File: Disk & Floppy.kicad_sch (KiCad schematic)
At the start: 13 parts, among them J7 Internal FDD, U18 74LS74, U19 74LS244, U20 74LS245, U21 74LS74, U22 74LS06, X1 8.010613MHz

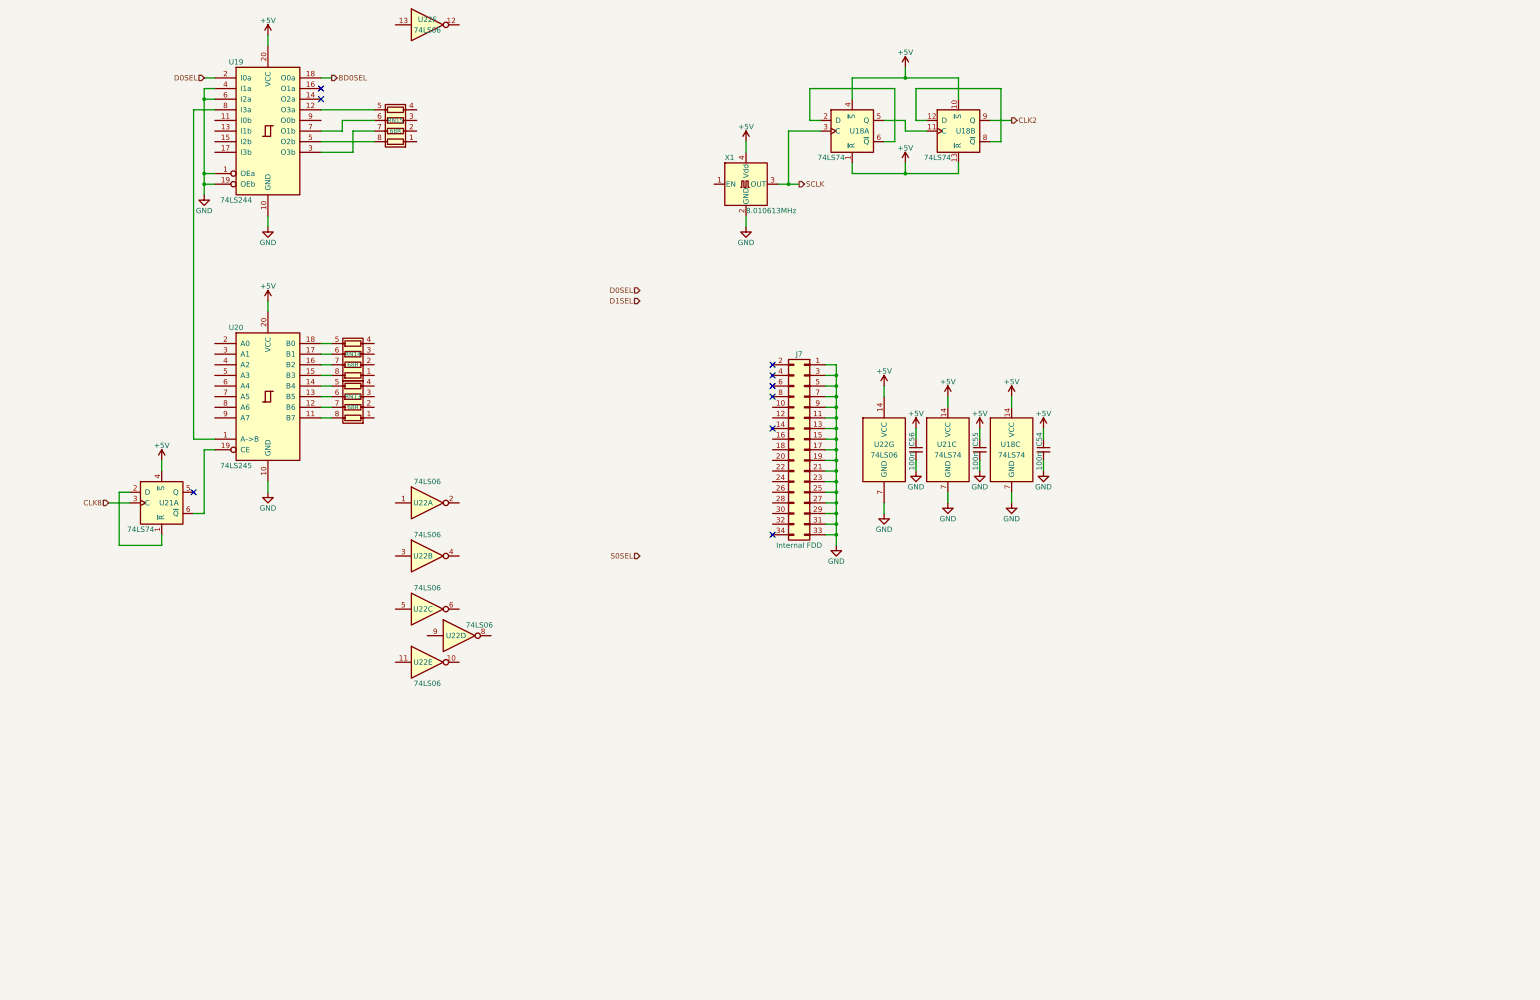
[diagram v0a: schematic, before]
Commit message: motherboard: Added the HDD and FDD controller logic to the schematic
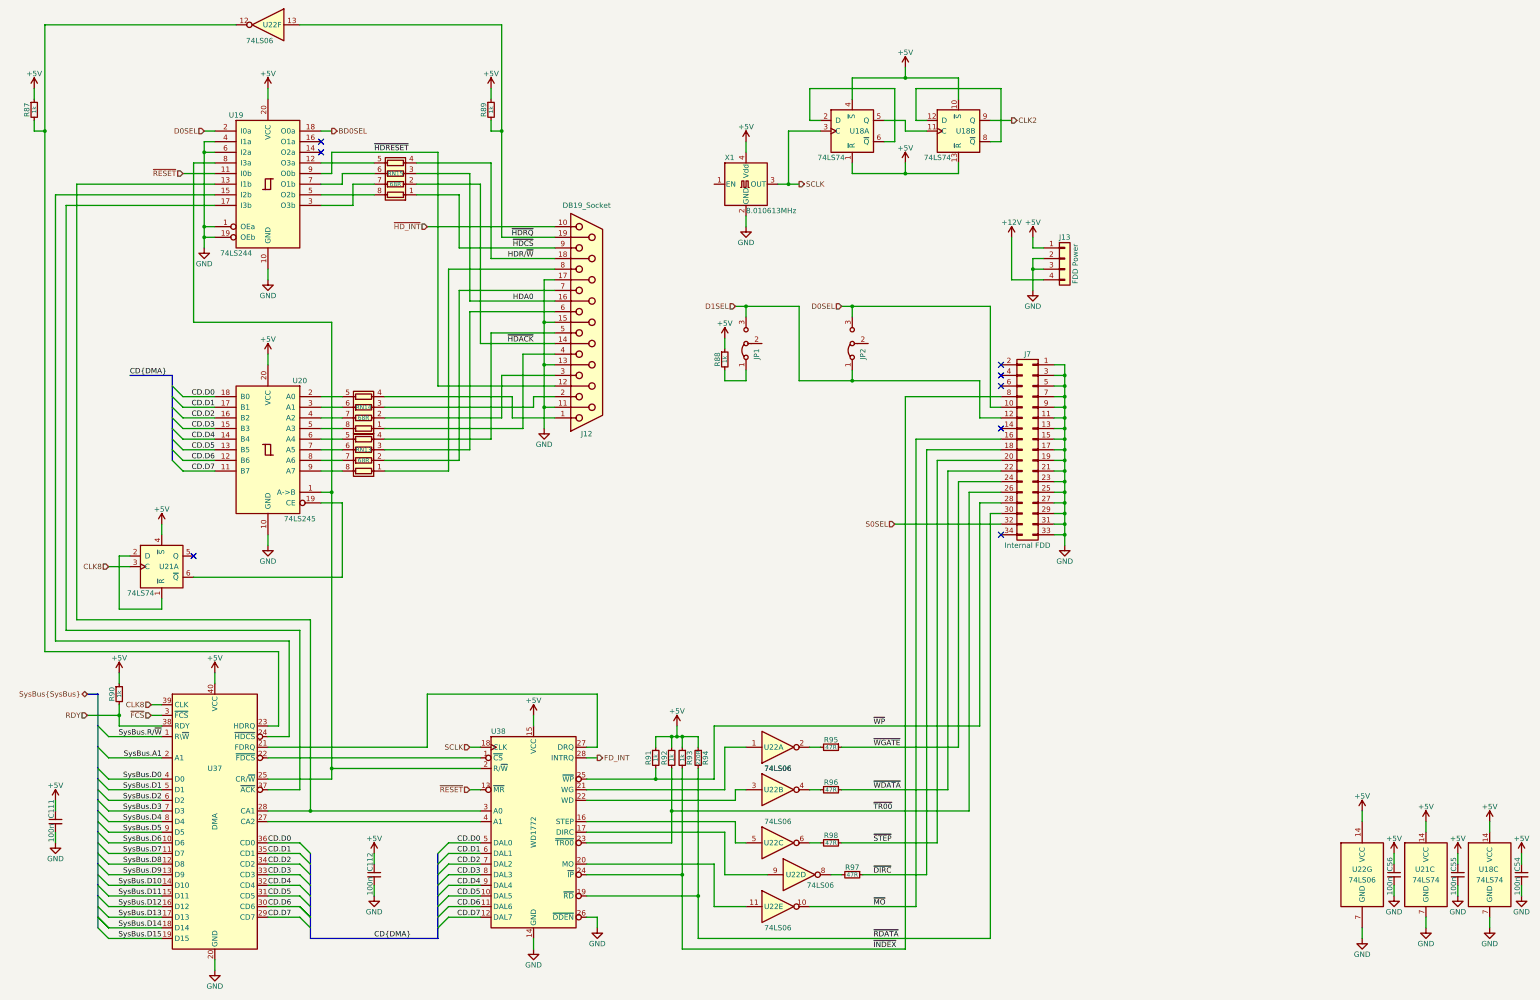
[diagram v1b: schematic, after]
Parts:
- added C111, C112: 100n, rhais_rcl:C0603, symbol Device:C_Small
- added J12: DB19_Socket, symbol dragonSTe:DB19_Socket
- added J13: FDD Power, symbol Connector_Generic:Conn_01x04
- added JP1, JP2: Jumper_3_Bridged12, symbol Jumper:Jumper_3_Bridged12
- added R87, R88, R89, R90, R91, R92, R93: 1k, rhais_rcl:R0603, symbol Device:R_Small
- added R94: 220R, rhais_rcl:R0603, symbol Device:R_Small
- added R95, R96, R97, R98: 47R, rhais_rcl:R0603, symbol Device:R_Small
- added U37: DMA, Package_DIP:DIP-40_W15.24mm_Socket, symbol dragonSTe:DMA
- added U38: WD1772, Package_DIP:DIP-28_W15.24mm_Socket, symbol dragonSTe:WD1772
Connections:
- net +5V: now also C111.1, C112.1, J13.1 (Pin_1), R87.1, R88.1, R89.1, R90.1, R91.1, R92.1, R93.1, R94.1, U37.40 (VCC), U38.15 (VCC)
- net CLK8: now also U37.39 (CLK)
- net D0SEL: now also J7.10 (Pin_10), JP2.3 (B)
- net D1SEL: now also J7.12 (Pin_12), JP1.3 (B), JP2.1 (A)
- net GND: now also C111.2, C112.2, J12.11, J12.13, J12.15 (P15), J12.17 (P17), J13.2 (Pin_2), J13.3 (Pin_3), U37.20 (GND), U37.28 (CA1), U38.14 (GND), U38.26 (~{DDEN})
- net S0SEL: now also J7.32 (Pin_32)
- net SCLK: now also U38.18 (CLK)
- net at U22.3: now also U38.22 (WD)
- net at U22.4: now also R96.2
- net ~{RESET}: now reaches U19.11 (I0b)
- net ~{RESET}: now also U38.13 (~{MR})
- net at U19.13 (I1b): now also U37.28 (CA1), U38.3 (A0)
- net at U19.15 (I2b): now also U37.24 (~{HDCS})
- net at U19.17 (I3b): now also U37.37 (~{ACK})
- net at U19.8 (I3a), U20.1 (A->B): now also U37.25 (CR/~{W}), U38.2 (R/~{W})
- net ~{HDRESET}: now reaches U19.9 (O0b)
- net ~{HDRESET}: now also J12.12
- net at RN13.8 (R1.2): now also U20.9 (A7); no longer U20.11 (B7)
- net at RN13.7 (R2.2): now also U20.8 (A6); no longer U20.12 (B6)
- net at RN13.6 (R3.2): now also U20.7 (A5); no longer U20.13 (B5)
- net at RN13.5 (R4.2): now also U20.6 (A4); no longer U20.14 (B4)
- net at RN14.8 (R1.2): now also U20.5 (A3); no longer U20.15 (B3)
- net at RN14.7 (R2.2): now also U20.4 (A2); no longer U20.16 (B2)
- net at RN14.6 (R3.2): now also U20.3 (A1); no longer U20.17 (B1)
- net at RN14.5 (R4.2): now also U20.2 (A0); no longer U20.18 (B0)
- net ~{MO}: now reaches U22.10
- net ~{MO}: now also J7.16 (Pin_16)
- net at U22.11: now also U38.20 (MO)
- net ~{HDCS}: now reaches RN15.1 (R1.1)
- net ~{HDCS}: now also J12.9
- net ~{HDACK}: now reaches RN15.2 (R2.1)
- net ~{HDACK}: now also J12.14 (P14)
- net HDA0: now reaches RN15.3 (R3.1)
- net HDA0: now also J12.16 (P16)
- net HDR/~{W}: now reaches RN15.4 (R4.1)
- net HDR/~{W}: now also J12.18 (P18)
- net at RN13.1 (R1.1): now also J12.8
- net at RN13.2 (R2.1): now also J12.7
- net at RN13.3 (R3.1): now also J12.6
- net at RN13.4 (R4.1): now also J12.5
- net at U22.5: now also U38.16 (STEP)
- net at U22.6: now also R98.2
- net at RN14.1 (R1.1): now also J12.4
- net at RN14.2 (R2.1): now also J12.3
- net at RN14.3 (R3.1): now also J12.2
- net at RN14.4 (R4.1): now also J12.1
- net at U22.12: now also R87.2, U37.23 (HDRQ)
- net ~{HDRQ}: now reaches U22.13
- net ~{HDRQ}: now also J12.19 (P19), R89.2
- net at U22.8: now also R97.2
- net at U22.9: now also U38.17 (DIRC)
- net ~{DIRC}: now reaches J7.18 (Pin_18)
- net ~{DIRC}: now also R97.1
- net ~{STEP}: now reaches J7.20 (Pin_20)
- net ~{STEP}: now also R98.1
- net ~{WDATA}: now reaches J7.22 (Pin_22)
- net ~{WDATA}: now also R96.1
- net ~{WGATE}: now reaches J7.24 (Pin_24)
- net ~{WGATE}: now also R95.1
- net ~{TR00}: now reaches J7.26 (Pin_26)
- net ~{TR00}: now also R92.2, U38.23 (~{TR00})
- net ~{WP}: now reaches J7.28 (Pin_28)
- net ~{WP}: now also R91.2, U38.25 (~{WP})
- net ~{RDATA}: now reaches J7.30 (Pin_30)
- net ~{RDATA}: now also R94.2, U38.19 (~{RD})
- net ~{INDEX}: now reaches J7.8 (Pin_8)
- net ~{INDEX}: now also R93.2, U38.24 (~{IP})
- net at U22.1: now also U38.21 (WG)
- net at U22.2: now also R95.2
- new net: JP1.1 (A), R88.2
- new net: U37.21 (FDRQ), U38.27 (DRQ)
- new net: U37.22 (~{FDCS}), U38.1 (~{CS})
- new net: U37.27 (CA2), U38.4 (A1)
- new net +12V: J13.4 (Pin_4)
- new net CD.D0: U20.18 (B0), U37.36 (CD0), U38.5 (DAL0)
- new net CD.D1: U20.17 (B1), U37.35 (CD1), U38.6 (DAL1)
- new net CD.D2: U20.16 (B2), U37.34 (CD2), U38.7 (DAL2)
- new net CD.D3: U20.15 (B3), U37.33 (CD3), U38.8 (DAL3)
- new net CD.D4: U20.14 (B4), U37.32 (CD4), U38.9 (DAL4)
- new net CD.D5: U20.13 (B5), U37.31 (CD5), U38.10 (DAL5)
- new net CD.D6: U20.12 (B6), U37.30 (CD6), U38.11 (DAL6)
- new net CD.D7: U20.11 (B7), U37.29 (CD7), U38.12 (DAL7)
- new net FD_INT: U38.28 (INTRQ)
- new net RDY: R90.2, U37.38 (RDY)
- new net SysBus.A1: U37.2 (A1)
- new net SysBus.D0: U37.4 (D0)
- new net SysBus.D1: U37.5 (D1)
- new net SysBus.D10: U37.14 (D10)
- new net SysBus.D11: U37.15 (D11)
- new net SysBus.D12: U37.16 (D12)
- new net SysBus.D13: U37.17 (D13)
- new net SysBus.D14: U37.18 (D14)
- new net SysBus.D15: U37.19 (D15)
- new net SysBus.D2: U37.6 (D2)
- new net SysBus.D3: U37.7 (D3)
- new net SysBus.D4: U37.8 (D4)
- new net SysBus.D5: U37.9 (D5)
- new net SysBus.D6: U37.10 (D6)
- new net SysBus.D7: U37.11 (D7)
- new net SysBus.D8: U37.12 (D8)
- new net SysBus.D9: U37.13 (D9)
- new net SysBus.R/~{W}: U37.1 (R\~{W})
- new net ~{FCS}: U37.3 (~{FCS})
- new net ~{HD_INT}: J12.10
- no-connect marks 9 -> 8
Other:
- moved on the sheet: C54, C55, C56, J7, RN13, RN14, RN15, U18C, U19, U20, U21A, U21C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

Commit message: motherboard: Added the BLiTTER to the schematic and tidied up a pile
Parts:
- J7: footprint (none) -> Connector_PinHeader_2.54mm:PinHeader_2x17_P2.54mm_Vertical
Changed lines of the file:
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@@
 			)
 		)
-		(property "Footprint" ""
+		(property "Footprint" "Connector_PinHeader_2.54mm:PinHeader_2x17_P2.54mm_Vertical"
 			(at 271.78 127 0)
 			(effects

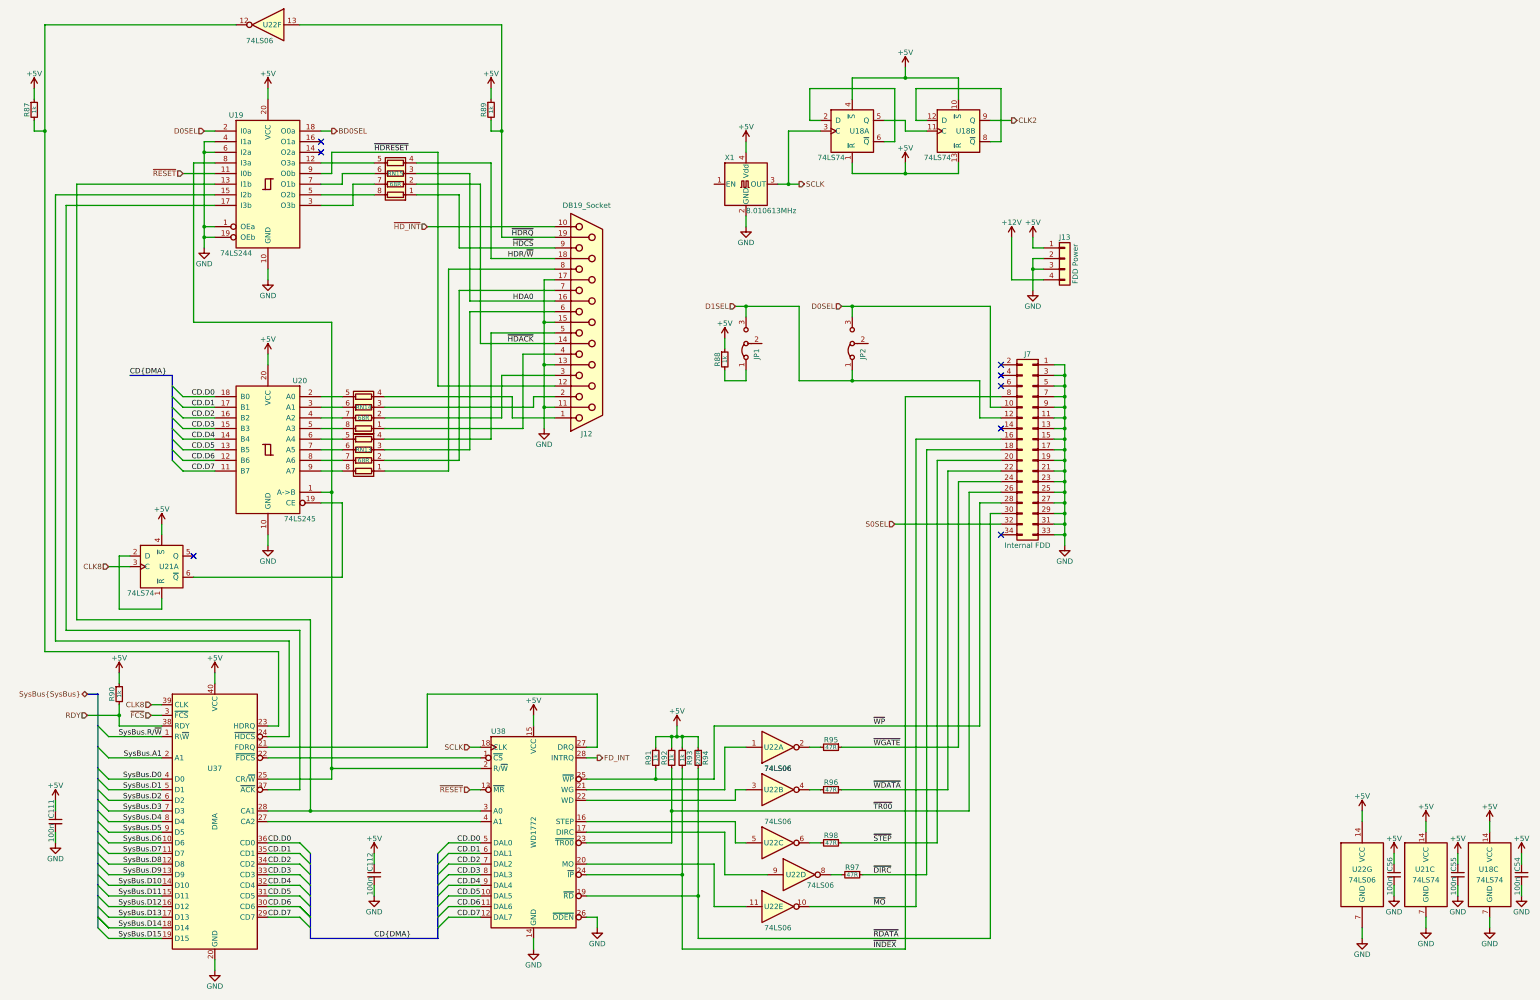
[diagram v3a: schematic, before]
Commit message: motherboard: More signal routing, and starting in on the BoM
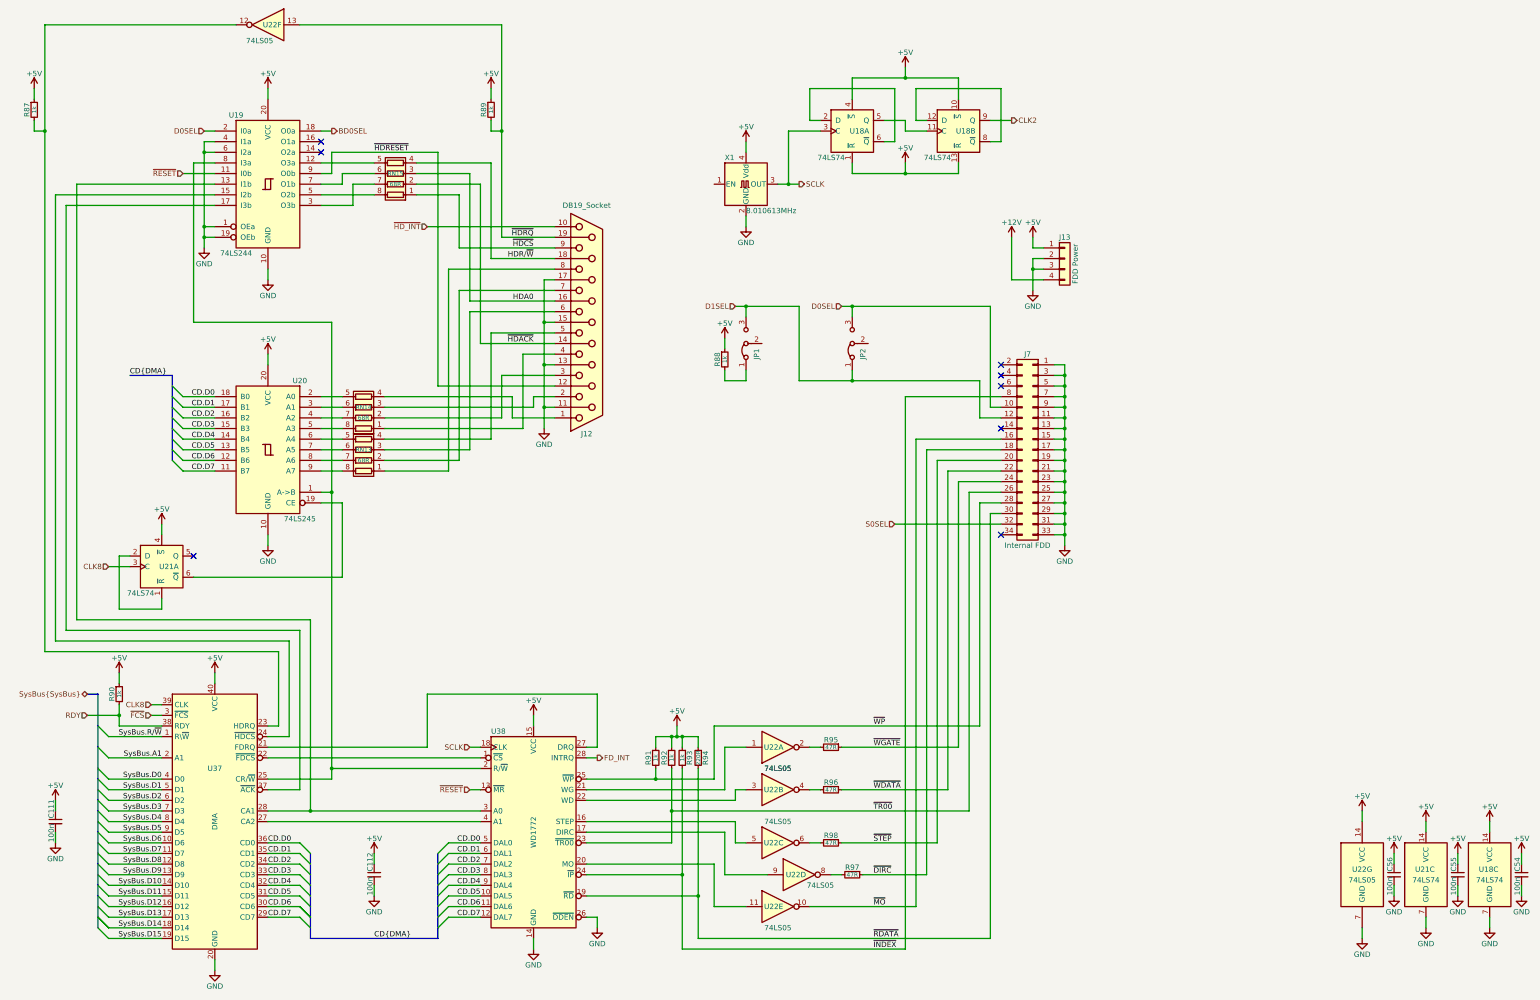
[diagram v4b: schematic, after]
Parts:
- U22: value 74LS06 -> 74LS05; footprint (none) -> Package_SO:SO-14_3.9x8.65mm_P1.27mm; MFR (none) -> TI; MPN (none) -> SN74HC05DR; OC_FARNELL (none) -> 3120437

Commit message: motherboard: Begun routing the internal floppy disk interface
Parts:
- J7: footprint Connector_PinHeader_2.54mm:PinHeader_2x17_P2.54mm_Vertical -> rhais_connector-pinheader:PinHeader_2x17_P2.54mm_Vertical
- U22: footprint Package_SO:SO-14_3.9x8.65mm_P1.27mm -> rhais_package-smd:SO-14_3.9x8.65mm_P1.27mm
- U37: footprint Package_DIP:DIP-40_W15.24mm_Socket -> rhais_package-dip:DIP-40_W15.24mm_Socket
- U38: footprint Package_DIP:DIP-28_W15.24mm_Socket -> rhais_package-dip:DIP-28_W15.24mm_Socket
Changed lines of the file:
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@@
 			)
 		)
-		(property "Footprint" "Package_SO:SO-14_3.9x8.65mm_P1.27mm"
+		(property "Footprint" "rhais_package-smd:SO-14_3.9x8.65mm_P1.27mm"
 			(at 210.82 208.28 0)
 			(effects
@@
 			)
 		)
-		(property "Footprint" "Package_SO:SO-14_3.9x8.65mm_P1.27mm"
+		(property "Footprint" "rhais_package-smd:SO-14_3.9x8.65mm_P1.27mm"
 			(at 210.82 236.22 0)
 			(effects
@@
 			)
 		)
-		(property "Footprint" "Package_SO:SO-14_3.9x8.65mm_P1.27mm"
+		(property "Footprint" "rhais_package-smd:SO-14_3.9x8.65mm_P1.27mm"
 			(at 210.82 220.98 0)
 			(effects
@@
 			)
 		)
-		(property "Footprint" "Package_SO:SO-14_3.9x8.65mm_P1.27mm"
+		(property "Footprint" "rhais_package-smd:SO-14_3.9x8.65mm_P1.27mm"
 			(at 88.9 25.4 0)
 			(effects
@@
 			)
 		)
-		(property "Footprint" "Package_SO:SO-14_3.9x8.65mm_P1.27mm"
+		(property "Footprint" "rhais_package-smd:SO-14_3.9x8.65mm_P1.27mm"
 			(at 215.9 228.6 0)
 			(effects
@@
 			)
 		)
-		(property "Footprint" "Package_DIP:DIP-40_W15.24mm_Socket"
+		(property "Footprint" "rhais_package-dip:DIP-40_W15.24mm_Socket"
 			(at 78.74 215.9 90)
 			(effects
@@
 			)
 		)
-		(property "Footprint" "Connector_PinHeader_2.54mm:PinHeader_2x17_P2.54mm_Vertical"
+		(property "Footprint" "rhais_connector-pinheader:PinHeader_2x17_P2.54mm_Vertical"
 			(at 271.78 127 0)
 			(effects
@@
 			)
 		)
-		(property "Footprint" "Package_SO:SO-14_3.9x8.65mm_P1.27mm"
+		(property "Footprint" "rhais_package-smd:SO-14_3.9x8.65mm_P1.27mm"
 			(at 210.82 198.12 0)
 			(effects
@@
 			)
 		)
-		(property "Footprint" "Package_DIP:DIP-28_W15.24mm_Socket"
+		(property "Footprint" "rhais_package-dip:DIP-28_W15.24mm_Socket"
 			(at 152.4 218.44 0)
 			(effects
@@
 			)
 		)
-		(property "Footprint" "Package_SO:SO-14_3.9x8.65mm_P1.27mm"
+		(property "Footprint" "rhais_package-smd:SO-14_3.9x8.65mm_P1.27mm"
 			(at 350.52 228.6 0)
 			(effects

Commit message: motherboard: Fixed the floppy power connector and defined the board parameters for manufacture
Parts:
- J12: value DB19_Socket -> External HDD
- J13: footprint (none) -> rhais_connector-pinheader:PinHeader_1x04_P2.54mm_Vertical
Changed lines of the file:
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@@
 			)
 		)
-		(property "Value" "DB19_Socket"
+		(property "Value" "External HDD"
 			(at 165.1 68.58 0)
 			(effects
@@
 			)
 		)
-		(property "Footprint" ""
+		(property "Footprint" "rhais_connector-pinheader:PinHeader_1x04_P2.54mm_Vertical"
 			(at 279.4 81.28 0)
 			(effects
